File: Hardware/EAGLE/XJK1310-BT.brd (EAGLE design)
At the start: 92 x 21 mm, 24 parts, among them IC1 74LVC1G08DCK, J2 10132797-011100LF, J3 10132798-011100LF, J4 61300911121, Q1 32.768, SW1 K3-2346D, U1 MDBT50Q, U2 3.3V

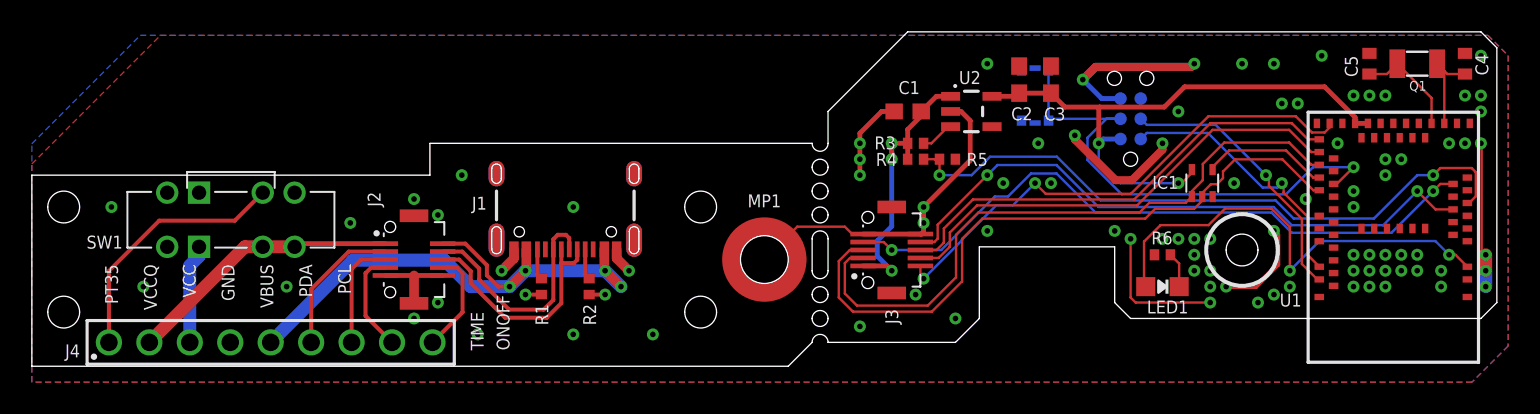
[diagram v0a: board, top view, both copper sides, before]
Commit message: Silkscreen change
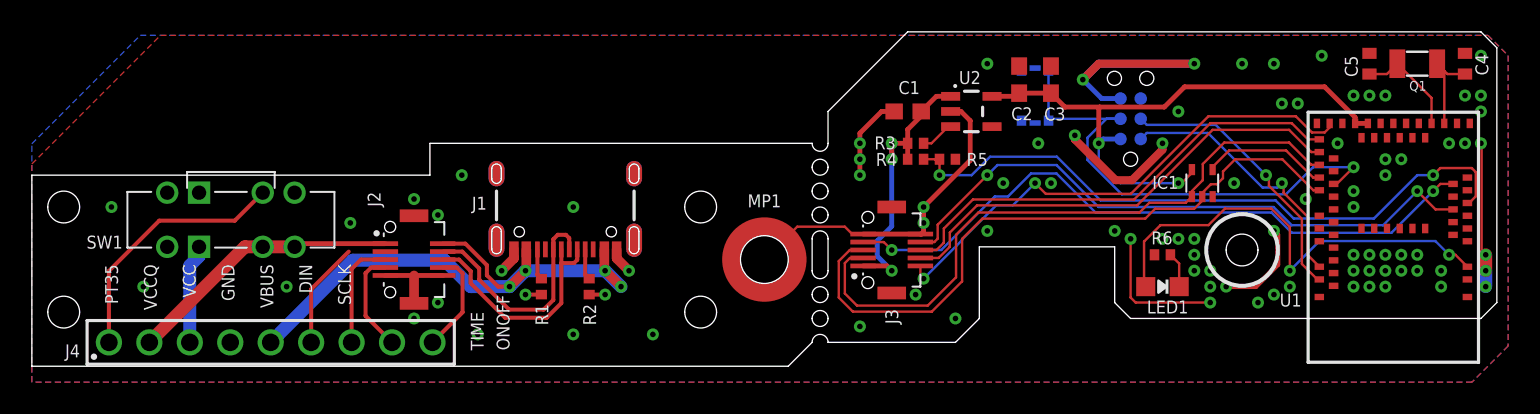
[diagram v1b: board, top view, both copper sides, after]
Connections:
- net PCL renamed SCLK
- net PDA renamed DIN
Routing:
- net DIN: track 49.5 -> 47.2 mm
- net GND: vias 92 -> 91
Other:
- board text added: "PT35 VCCQ VCC GND VBUS DIN SCLK"
- board text removed: "PT35 VCCQ VCC GND VBUS PDA PCL"
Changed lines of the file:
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@@
 GND
 VBUS
-PDA
-PCL</text>
+DIN
+SCLK</text>
 <text x="30" y="1" size="0.8128" layer="21" distance="100" rot="R90">TIME
 ONOFF</text>
@@
 <via x="66" y="18" extent="1-16" drill="0.35"/>
 <via x="65.5" y="14.5" extent="1-16" drill="0.35"/>
-<via x="74" y="8" extent="1-16" drill="0.35"/>
 <via x="69" y="8" extent="1-16" drill="0.35"/>
 <via x="71" y="14" extent="1-16" drill="0.35"/>
@@
 <via x="55.5" y="4.5" extent="1-16" drill="0.35"/>
 <contactref element="IC1" pad="3"/>
-<wire x1="66" y1="18" x2="66.796" y2="18.796" width="0.508" layer="1"/>
-<wire x1="72.796" y1="18.796" x2="73" y2="19" width="0.508" layer="1"/>
-<wire x1="66.796" y1="18.796" x2="72.796" y2="18.796" width="0.508" layer="1"/>
-<wire x1="66" y1="18" x2="66.796" y2="18.796" width="0.508" layer="16"/>
-<wire x1="72.796" y1="18.796" x2="73" y2="19" width="0.508" layer="16"/>
-<wire x1="66.796" y1="18.796" x2="72.796" y2="18.796" width="0.508" layer="16"/>
+<wire x1="67" y1="19" x2="66" y2="18" width="0.508" layer="1"/>
+<wire x1="67" y1="19" x2="73" y2="19" width="0.508" layer="1"/>
+<wire x1="67" y1="19" x2="73" y2="19" width="0.508" layer="16"/>
+<wire x1="67" y1="19" x2="66" y2="18" width="0.508" layer="16"/>
 <wire x1="65.5" y1="14.5" x2="65.5" y2="14.246" width="0.508" layer="1"/>
 <wire x1="68.062" y1="11.684" x2="65.5" y2="14.246" width="0.508" layer="1"/>
@@
 <contactref element="S1" pad="3"/>
 <contactref element="S1" pad="5"/>
-<wire x1="52.2" y1="8.3" x2="51.562" y2="8.255" width="0" layer="19" extent="1-1"/>
+<wire x1="51.562" y1="8.255" x2="52.2" y2="8.3" width="0" layer="19" extent="1-1"/>
 </signal>
 <signal name="VBUS">
@@
 <wire x1="34.75" y1="5.75" x2="35" y2="5.5" width="0.254" layer="1"/>
 </signal>
-<signal name="PDA">
-<contactref element="J4" pad="6"/>
-<contactref element="J2" pad="2"/>
-<wire x1="22.2" y1="7.2" x2="19.9" y2="7.2" width="0.254" layer="1"/>
-<wire x1="17.54" y1="4.84" x2="17.54" y2="1.5" width="0.254" layer="1"/>
-<wire x1="19.9" y1="7.2" x2="17.54" y2="4.84" width="0.254" layer="1"/>
-<contactref element="J3" pad="2"/>
-<contactref element="U1" pad="37"/>
-<wire x1="80.85" y1="12.65" x2="80.35" y2="12.65" width="0.1524" layer="1"/>
-<wire x1="80.35" y1="12.65" x2="78.953" y2="14.047" width="0.1524" layer="1"/>
-<wire x1="78.953" y1="14.047" x2="74.88" y2="14.047" width="0.1524" layer="1"/>
-<wire x1="59.436" y1="9.652" x2="58.039" y2="8.255" width="0.1524" layer="1"/>
-<wire x1="58.039" y1="8.255" x2="58.039" y2="5.588" width="0.1524" layer="1"/>
-<wire x1="58.039" y1="5.588" x2="56.261" y2="3.81" width="0.1524" layer="1"/>
-<wire x1="56.261" y1="3.81" x2="51.816" y2="3.81" width="0.1524" layer="1"/>
-<wire x1="51.054" y1="4.572" x2="51.054" y2="6.477" width="0.1524" layer="1"/>
-<wire x1="51.054" y1="6.477" x2="51.377" y2="6.8" width="0.1524" layer="1"/>
-<wire x1="51.377" y1="6.8" x2="52.2" y2="6.8" width="0.1524" layer="1"/>
-<wire x1="51.816" y1="3.81" x2="51.054" y2="4.572" width="0.1524" layer="1"/>
-<contactref element="IC1" pad="1"/>
-<wire x1="72.85" y1="10.65" x2="72.469" y2="10.269" width="0.1524" layer="1"/>
-<wire x1="72.469" y1="10.269" x2="70.175" y2="10.269" width="0.1524" layer="1"/>
-<wire x1="70.175" y1="10.269" x2="69.558" y2="9.652" width="0.1524" layer="1"/>
-<wire x1="69.558" y1="9.652" x2="59.436" y2="9.652" width="0.1524" layer="1"/>
-<wire x1="73.533" y1="11.684" x2="72.85" y2="11.001" width="0.1524" layer="1"/>
-<wire x1="72.85" y1="10.65" x2="72.85" y2="11.001" width="0.1524" layer="1"/>
-<wire x1="73.533" y1="11.684" x2="73.533" y2="12.7" width="0.1524" layer="1"/>
-<wire x1="73.533" y1="12.7" x2="74.88" y2="14.047" width="0.1524" layer="1"/>
-<wire x1="22.2" y1="7.2" x2="52.2" y2="6.8" width="0" layer="19" extent="1-1"/>
-</signal>
-<signal name="PCL">
+<signal name="SCLK">
 <contactref element="J4" pad="7"/>
 <contactref element="J2" pad="3"/>
@@
 <wire x1="72.05" y1="6.45" x2="71.5" y2="7" width="0.1524" layer="1"/>
 </signal>
+<signal name="DIN">
+<contactref element="J2" pad="2"/>
+<contactref element="J4" pad="6"/>
+<wire x1="17.54" y1="4.84" x2="17.54" y2="1.5" width="0.254" layer="1"/>
+<wire x1="19.9" y1="7.2" x2="17.54" y2="4.84" width="0.254" layer="1"/>
+<contactref element="J3" pad="2"/>
+<contactref element="U1" pad="37"/>
+<wire x1="80.85" y1="12.65" x2="80.35" y2="12.65" width="0.1524" layer="1"/>
+<wire x1="80.35" y1="12.65" x2="78.953" y2="14.047" width="0.1524" layer="1"/>
+<wire x1="78.953" y1="14.047" x2="74.88" y2="14.047" width="0.1524" layer="1"/>
+<wire x1="59.436" y1="9.652" x2="58.039" y2="8.255" width="0.1524" layer="1"/>
+<wire x1="58.039" y1="8.255" x2="58.039" y2="5.588" width="0.1524" layer="1"/>
+<wire x1="58.039" y1="5.588" x2="56.261" y2="3.81" width="0.1524" layer="1"/>
+<wire x1="56.261" y1="3.81" x2="51.816" y2="3.81" width="0.1524" layer="1"/>
+<wire x1="51.054" y1="4.572" x2="51.054" y2="6.477" width="0.1524" layer="1"/>
+<wire x1="51.054" y1="6.477" x2="51.377" y2="6.8" width="0.1524" layer="1"/>
+<wire x1="51.377" y1="6.8" x2="52.2" y2="6.8" width="0.1524" layer="1"/>
+<wire x1="51.816" y1="3.81" x2="51.054" y2="4.572" width="0.1524" layer="1"/>
+<contactref element="IC1" pad="1"/>
+<wire x1="72.85" y1="10.65" x2="72.469" y2="10.269" width="0.1524" layer="1"/>
+<wire x1="72.469" y1="10.269" x2="70.175" y2="10.269" width="0.1524" layer="1"/>
+<wire x1="70.175" y1="10.269" x2="69.558" y2="9.652" width="0.1524" layer="1"/>
+<wire x1="69.558" y1="9.652" x2="59.436" y2="9.652" width="0.1524" layer="1"/>
+<wire x1="73.533" y1="11.684" x2="72.85" y2="11.001" width="0.1524" layer="1"/>
+<wire x1="72.85" y1="10.65" x2="72.85" y2="11.001" width="0.1524" layer="1"/>
+<wire x1="73.533" y1="11.684" x2="73.533" y2="12.7" width="0.1524" layer="1"/>
+<wire x1="73.533" y1="12.7" x2="74.88" y2="14.047" width="0.1524" layer="1"/>
+<wire x1="22.2" y1="7.2" x2="52.2" y2="6.8" width="0" layer="19" extent="1-1"/>
+<wire x1="19.9" y1="7.2" x2="22.2" y2="7.2" width="0" layer="19" extent="1-1"/>
+</signal>
 </signals>
